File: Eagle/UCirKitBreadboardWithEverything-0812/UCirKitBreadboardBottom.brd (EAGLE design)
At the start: 64.8 x 99.4 mm, 900 parts

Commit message: 100% Bottom PCB
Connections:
- removed net 0_1439393321: JP661.P$2
- removed net 0_1439394245: JP601.P$2
- removed net N$1000: JP1000.P$2
- removed net N$1001: JP1001.P$2
- removed net N$1002: JP1002.P$2
- removed net N$1003: JP1003.P$2
- removed net N$1004: JP1004.P$2
- removed net N$1007: JP1007.P$2
- removed net N$1008: JP1008.P$2
- removed net N$1009: JP1009.P$2
- removed net N$1010: JP1010.P$2
- removed net N$1011: JP1011.P$2
- removed net N$1012: JP1012.P$2
- removed net N$1013: JP1013.P$2
- removed net N$1014: JP1014.P$2
- removed net N$1015: JP1015.P$2
- removed net N$1016: JP1016.P$2
- removed net N$1017: JP1017.P$2
- removed net N$1018: JP1018.P$2
- removed net N$1019: JP1019.P$2
- removed net N$1020: JP1020.P$2
- removed net N$1021: JP1021.P$2
- removed net N$1022: JP1022.P$2
- removed net N$1023: JP1023.P$2
- removed net N$1024: JP1024.P$2
- removed net N$1025: JP1025.P$2
- removed net N$1026: JP1026.P$2
- removed net N$1027: JP1027.P$2
- removed net N$1028: JP1028.P$2
- removed net N$1029: JP1029.P$2
- removed net N$1030: JP1030.P$2
- removed net N$1031: JP1031.P$2
- removed net N$1032: JP1032.P$2
- removed net N$1033: JP1033.P$2
- removed net N$1034: JP1034.P$2
- removed net N$1035: JP1035.P$2
- removed net N$1036: JP1036.P$2
- removed net N$1037: JP1037.P$2
- removed net N$1038: JP1038.P$2
- removed net N$1039: JP1039.P$2
- removed net N$1040: JP1040.P$2
- removed net N$1041: JP1041.P$2
- removed net N$1042: JP1042.P$2
- removed net N$1043: JP1043.P$2
- removed net N$1044: JP1044.P$2
- removed net N$1045: JP1045.P$2
- removed net N$1046: JP1046.P$2
- removed net N$1047: JP1047.P$2
- removed net N$1048: JP1048.P$2
- removed net N$1049: JP1049.P$2
- removed net N$1050: JP1050.P$2
- removed net N$1051: JP1051.P$2
- removed net N$1052: JP1052.P$2
- removed net N$1053: JP1053.P$2
- removed net N$1054: JP1054.P$2
- removed net N$1055: JP1055.P$2
- removed net N$1056: JP1056.P$2
- removed net N$1057: JP1057.P$2
- removed net N$1058: JP1058.P$2
- removed net N$1059: JP1059.P$2
- removed net N$1060: JP1060.P$2
- removed net N$1061: JP1061.P$2
- removed net N$1062: JP1062.P$2
- removed net N$1063: JP1063.P$2
- removed net N$1064: JP1064.P$2
- removed net N$1065: JP1065.P$2
- removed net N$1066: JP1066.P$2
- removed net N$1067: JP1067.P$2
- removed net N$1068: JP1068.P$2
- removed net N$1069: JP1069.P$2
- removed net N$1070: JP1070.P$2
- removed net N$1071: JP1071.P$2
- removed net N$1072: JP1072.P$2
- removed net N$1073: JP1073.P$2
- removed net N$1074: JP1074.P$2
- removed net N$1075: JP1075.P$2
- removed net N$1076: JP1076.P$2
- removed net N$1077: JP1077.P$2
- removed net N$1078: JP1078.P$2
- removed net N$1079: JP1079.P$2
- removed net N$1080: JP1080.P$2
- removed net N$1081: JP1081.P$2
- removed net N$1082: JP1082.P$2
- removed net N$1083: JP1083.P$2
- removed net N$1084: JP1084.P$2
- removed net N$1085: JP1085.P$2
- removed net N$1086: JP1086.P$2
- removed net N$1087: JP1087.P$2
- removed net N$1088: JP1088.P$2
- removed net N$1089: JP1089.P$2
- removed net N$1090: JP1090.P$2
- removed net N$1091: JP1091.P$2
- removed net N$1092: JP1092.P$2
- removed net N$1093: JP1093.P$2
- removed net N$1094: JP1094.P$2
- removed net N$1095: JP1095.P$2
- removed net N$1096: JP1096.P$2
- removed net N$1097: JP1097.P$2
- removed net N$1098: JP1098.P$2
- removed net N$1099: JP1099.P$2
- removed net N$1100: JP1100.P$2
- removed net N$1101: JP1101.P$2
- removed net N$1102: JP1102.P$2
- removed net N$1103: JP1103.P$2
- removed net N$1104: JP1104.P$2
- removed net N$1105: JP1105.P$2
- removed net N$1106: JP1106.P$2
- removed net N$1107: JP1107.P$2
- removed net N$1108: JP1108.P$2
- removed net N$1109: JP1109.P$2
- removed net N$1110: JP1110.P$2
- removed net N$1111: JP1111.P$2
- removed net N$1112: JP1112.P$2
- removed net N$1113: JP1113.P$2
- removed net N$1114: JP1114.P$2
- removed net N$1115: JP1115.P$2
- removed net N$1116: JP1116.P$2
- removed net N$1117: JP1117.P$2
- removed net N$1118: JP1118.P$2
- removed net N$1119: JP1119.P$2
- removed net N$1120: JP1120.P$2
- removed net N$1121: JP1121.P$2
- removed net N$1122: JP1122.P$2
- removed net N$1123: JP1123.P$2
- removed net N$1124: JP1124.P$2
- removed net N$1125: JP1125.P$2
- removed net N$1126: JP1126.P$2
- removed net N$1127: JP1127.P$2
- removed net N$1128: JP1128.P$2
- removed net N$1129: JP1129.P$2
- removed net N$1130: JP1130.P$2
- removed net N$1131: JP1131.P$2
- removed net N$1132: JP1132.P$2
- removed net N$1133: JP1133.P$2
- removed net N$1134: JP1134.P$2
- removed net N$1135: JP1135.P$2
- removed net N$1136: JP1136.P$2
- removed net N$1137: JP1137.P$2
- removed net N$1138: JP1138.P$2
- removed net N$1139: JP1139.P$2
- removed net N$1140: JP1140.P$2
- removed net N$1141: JP1141.P$2
- removed net N$1142: JP1142.P$2
- removed net N$1143: JP1143.P$2
- removed net N$1144: JP1144.P$2
- removed net N$1145: JP1145.P$2
- removed net N$1146: JP1146.P$2
- removed net N$1147: JP1147.P$2
- removed net N$1148: JP1148.P$2
- removed net N$1149: JP1149.P$2
- removed net N$1150: JP1150.P$2
- removed net N$1151: JP1151.P$2
- removed net N$1152: JP1152.P$2
- removed net N$1153: JP1153.P$2
- removed net N$1154: JP1154.P$2
- removed net N$1155: JP1155.P$2
- removed net N$1156: JP1156.P$2
- removed net N$1157: JP1157.P$2
- removed net N$1158: JP1158.P$2
- removed net N$1159: JP1159.P$2
- removed net N$1160: JP1160.P$2
- removed net N$1161: JP1161.P$2
- removed net N$1162: JP1162.P$2
- removed net N$1163: JP1163.P$2
- removed net N$1164: JP1164.P$2
- removed net N$1165: JP1165.P$2
- removed net N$1166: JP1166.P$2
- removed net N$1167: JP1167.P$2
- removed net N$1168: JP1168.P$2
- removed net N$1169: JP1169.P$2
- removed net N$1170: JP1170.P$2
- removed net N$1171: JP1171.P$2
- removed net N$1172: JP1172.P$2
- removed net N$1173: JP1173.P$2
- removed net N$1174: JP1174.P$2
- removed net N$1175: JP1175.P$2
- removed net N$1176: JP1176.P$2
- removed net N$1177: JP1177.P$2
- removed net N$1178: JP1178.P$2
- removed net N$1179: JP1179.P$2
- removed net N$1180: JP1180.P$2
- removed net N$1181: JP1181.P$2
- removed net N$1182: JP1182.P$2
- removed net N$1183: JP1183.P$2
- removed net N$1184: JP1184.P$2
- removed net N$1185: JP1185.P$2
- removed net N$1186: JP1186.P$2
- removed net N$1187: JP1187.P$2
- removed net N$1188: JP1188.P$2
- removed net N$1189: JP1189.P$2
- removed net N$1190: JP1190.P$2
- removed net N$1191: JP1191.P$2
- removed net N$1192: JP1192.P$2
- removed net N$1193: JP1193.P$2
- removed net N$1194: JP1194.P$2
- removed net N$1195: JP1195.P$2
- removed net N$1196: JP1196.P$2
- removed net N$1197: JP1197.P$2
- removed net N$1198: JP1198.P$2
- removed net N$1199: JP1199.P$2
- removed net N$1200: JP1200.P$2
- removed net N$902: JP902.P$2
- removed net N$903: JP903.P$2
- removed net N$904: JP904.P$2
- removed net N$905: JP905.P$2
- removed net N$906: JP906.P$2
- removed net N$907: JP907.P$2
- removed net N$908: JP908.P$2
- removed net N$909: JP909.P$2
- removed net N$910: JP910.P$2
- removed net N$911: JP911.P$2
- removed net N$912: JP912.P$2
- removed net N$913: JP913.P$2
- removed net N$914: JP914.P$2
- removed net N$915: JP915.P$2
- removed net N$916: JP916.P$2
- removed net N$917: JP917.P$2
- removed net N$918: JP918.P$2
- removed net N$919: JP919.P$2
- removed net N$920: JP920.P$2
- removed net N$921: JP921.P$2
- removed net N$922: JP922.P$2
- removed net N$923: JP923.P$2
- removed net N$924: JP924.P$2
- removed net N$925: JP925.P$2
- removed net N$926: JP926.P$2
- removed net N$927: JP927.P$2
- removed net N$928: JP928.P$2
- removed net N$929: JP929.P$2
- removed net N$930: JP930.P$2
- removed net N$931: JP931.P$2
- removed net N$932: JP932.P$2
- removed net N$933: JP933.P$2
- removed net N$934: JP934.P$2
- removed net N$935: JP935.P$2
- removed net N$936: JP936.P$2
- removed net N$937: JP937.P$2
- removed net N$938: JP938.P$2
- removed net N$939: JP939.P$2
- removed net N$940: JP940.P$2
- removed net N$941: JP941.P$2
- removed net N$942: JP942.P$2
- removed net N$943: JP943.P$2
- removed net N$944: JP944.P$2
- removed net N$945: JP945.P$2
- removed net N$946: JP946.P$2
- removed net N$947: JP947.P$2
- removed net N$948: JP948.P$2
- removed net N$949: JP949.P$2
- removed net N$950: JP950.P$2
- removed net N$951: JP951.P$2
- removed net N$952: JP952.P$2
- removed net N$953: JP953.P$2
- removed net N$954: JP954.P$2
- removed net N$955: JP955.P$2
- removed net N$956: JP956.P$2
- removed net N$957: JP957.P$2
- removed net N$958: JP958.P$2
- removed net N$959: JP959.P$2
- removed net N$960: JP960.P$2
- removed net N$962: JP962.P$2
- removed net N$963: JP963.P$2
- removed net N$964: JP964.P$2
- removed net N$965: JP965.P$2
- removed net N$966: JP966.P$2
- removed net N$967: JP967.P$2
- removed net N$968: JP968.P$2
- removed net N$969: JP969.P$2
- removed net N$970: JP970.P$2
- removed net N$971: JP971.P$2
- removed net N$972: JP972.P$2
- removed net N$973: JP973.P$2
- removed net N$974: JP974.P$2
- removed net N$975: JP975.P$2
- removed net N$976: JP976.P$2
- removed net N$977: JP977.P$2
- removed net N$978: JP978.P$2
- removed net N$979: JP979.P$2
- removed net N$980: JP980.P$2
- removed net N$981: JP981.P$2
- removed net N$982: JP982.P$2
- removed net N$983: JP983.P$2
- removed net N$984: JP984.P$2
- removed net N$985: JP985.P$2
- removed net N$986: JP986.P$2
- removed net N$987: JP987.P$2
- removed net N$988: JP988.P$2
- removed net N$989: JP989.P$2
- removed net N$990: JP990.P$2
- removed net N$991: JP991.P$2
- removed net N$992: JP992.P$2
- removed net N$993: JP993.P$2
- removed net N$994: JP994.P$2
- removed net N$995: JP995.P$2
- removed net N$996: JP996.P$2
- removed net N$997: JP997.P$2
- removed net N$998: JP998.P$2
- removed net N$999: JP999.P$2
- net 0_1439393083: now also JP1019.P$2
- net 0_1439393096: now also JP1017.P$2
- net 0_1439393111: now also JP1015.P$2
- net 0_1439393132: now also JP1005.P$2
- net 0_1439393222: now also JP1013.P$2
- net 0_1439393235: now also JP1011.P$2
- net 0_1439393247: now also JP1009.P$2
- net 0_1439393259: now also JP1007.P$2
- net 0_1439393301: now also JP1006.P$2
- net 0_1439393535: now also JP1003.P$2
- net 0_1439393546: now also JP1001.P$2
- net 0_1439393557: now also JP999.P$2
- net 0_1439393568: now also JP997.P$2
- net 0_1439393578: now also JP995.P$2
- net 0_1439393590: now also JP993.P$2
- net 0_1439393601: now also JP991.P$2
- net 0_1439393611: now also JP989.P$2
- net 0_1439393621: now also JP987.P$2
- net 0_1439393632: now also JP985.P$2
- net 0_1439393643: now also JP983.P$2
- net 0_1439393653: now also JP981.P$2
- net 0_1439393662: now also JP979.P$2
- net 0_1439393672: now also JP977.P$2
- net 0_1439393682: now also JP975.P$2
- net 0_1439393692: now also JP973.P$2
- net 0_1439393702: now also JP971.P$2
- net 0_1439393713: now also JP969.P$2
- net 0_1439393723: now also JP967.P$2
- net 0_1439393733: now also JP965.P$2
- net 0_1439393743: now also JP963.P$2
- net 0_1439393751: now also JP962.P$2
- net 0_1439394322: now also JP1141.P$2
- net 0_1439394368: now also JP1021.P$2
- net 0_1439394379: now also JP1023.P$2
- net 0_1439394391: now also JP1025.P$2
- net 0_1439394441: now also JP1027.P$2
- net 0_1439394451: now also JP1029.P$2
- net 0_1439394459: now also JP1031.P$2
- net 0_1439394467: now also JP1033.P$2
- net 0_1439394476: now also JP1035.P$2
- net 0_1439394485: now also JP1037.P$2
- net 0_1439394493: now also JP1039.P$2
- net 0_1439394502: now also JP1041.P$2
- net 0_1439394512: now also JP1043.P$2
- net 0_1439394521: now also JP1045.P$2
- net 0_1439394528: now also JP1047.P$2
- net 0_1439394536: now also JP1049.P$2
- net 0_1439394545: now also JP1051.P$2
- net 0_1439394554: now also JP1053.P$2
- net 0_1439394565: now also JP1055.P$2
- net 0_1439394575: now also JP1057.P$2
- net 0_1439394583: now also JP1059.P$2
- net 0_1439394592: now also JP1061.P$2
- net 0_1439394601: now also JP1063.P$2
- net 0_1439394609: now also JP1065.P$2
- net 0_1439394617: now also JP1067.P$2
- net 0_1439394705: now also JP1069.P$2
- net 0_1439394717: now also JP1071.P$2
- net 0_1439394727: now also JP1073.P$2
- net 0_1439394736: now also JP1075.P$2
- net 0_1439394745: now also JP1077.P$2
- net 0_1439394755: now also JP1079.P$2
- net 0_1439394769: now also JP1181.P$2
- net 0_1439394798: now also JP1161.P$2
- net 0_1439394824: now also JP1191.P$2
- net 0_1439394861: now also JP902.P$2
- net 0_1439394997: now also JP1081.P$2
- net 10_1439394322: now also JP1151.P$2
- net 10_1439394798: now also JP1171.P$2
- net 10_1439394861: now also JP912.P$2
- net 10_1439394997: now also JP1091.P$2
- net 11_1439394322: now also JP1152.P$2
- net 11_1439394798: now also JP1172.P$2
- net 11_1439394861: now also JP913.P$2
- net 11_1439394997: now also JP1092.P$2
- net 12_1439394322: now also JP1153.P$2
- net 12_1439394798: now also JP1173.P$2
- net 12_1439394861: now also JP914.P$2
- net 12_1439394997: now also JP1093.P$2
- net 13_1439394322: now also JP1154.P$2
- net 13_1439394798: now also JP1174.P$2
- net 13_1439394861: now also JP915.P$2
- net 13_1439394997: now also JP1094.P$2
- net 14_1439394322: now also JP1155.P$2
- net 14_1439394798: now also JP1175.P$2
- net 14_1439394861: now also JP916.P$2
- net 14_1439394997: now also JP1095.P$2
- net 15_1439394322: now also JP1156.P$2
- net 15_1439394798: now also JP1176.P$2
- net 15_1439394861: now also JP917.P$2
- net 15_1439394997: now also JP1096.P$2
- net 16_1439394322: now also JP1157.P$2
- net 16_1439394798: now also JP1177.P$2
- net 16_1439394861: now also JP918.P$2
- net 16_1439394997: now also JP1097.P$2
- net 17_1439394322: now also JP1158.P$2
- net 17_1439394798: now also JP1178.P$2
- net 17_1439394861: now also JP919.P$2
- net 17_1439394997: now also JP1098.P$2
- net 18_1439394322: now also JP1159.P$2
- net 18_1439394798: now also JP1179.P$2
- net 18_1439394861: now also JP920.P$2
- net 18_1439394997: now also JP1099.P$2
- net 19_1439394322: now also JP1160.P$2
- net 19_1439394798: now also JP1180.P$2
- net 19_1439394861: now also JP921.P$2
- net 19_1439394997: now also JP1100.P$2
- net 1_1439393083: now also JP1020.P$2
- net 1_1439393096: now also JP1018.P$2
- net 1_1439393111: now also JP1016.P$2
- net 1_1439393222: now also JP1014.P$2
- net 1_1439393235: now also JP1012.P$2
- net 1_1439393247: now also JP1010.P$2
- net 1_1439393259: now also JP1008.P$2
- net 1_1439393535: now also JP1004.P$2
- net 1_1439393546: now also JP1002.P$2
- net 1_1439393557: now also JP1000.P$2
- net 1_1439393568: now also JP998.P$2
- net 1_1439393578: now also JP996.P$2
- net 1_1439393590: now also JP994.P$2
- net 1_1439393601: now also JP992.P$2
- net 1_1439393611: now also JP990.P$2
- net 1_1439393621: now also JP988.P$2
- net 1_1439393632: now also JP986.P$2
- net 1_1439393643: now also JP984.P$2
- net 1_1439393653: now also JP982.P$2
- net 1_1439393662: now also JP980.P$2
- net 1_1439393672: now also JP978.P$2
- net 1_1439393682: now also JP976.P$2
- net 1_1439393692: now also JP974.P$2
- net 1_1439393702: now also JP972.P$2
- net 1_1439393713: now also JP970.P$2
- net 1_1439393723: now also JP968.P$2
- net 1_1439393733: now also JP966.P$2
- net 1_1439393743: now also JP964.P$2
- net 1_1439394322: now also JP1142.P$2
- net 1_1439394368: now also JP1022.P$2
- net 1_1439394379: now also JP1024.P$2
- net 1_1439394391: now also JP1026.P$2
- net 1_1439394441: now also JP1028.P$2
- net 1_1439394451: now also JP1030.P$2
- net 1_1439394459: now also JP1032.P$2
- net 1_1439394467: now also JP1034.P$2
- net 1_1439394476: now also JP1036.P$2
- net 1_1439394485: now also JP1038.P$2
- net 1_1439394493: now also JP1040.P$2
- net 1_1439394502: now also JP1042.P$2
- net 1_1439394512: now also JP1044.P$2
- net 1_1439394521: now also JP1046.P$2
- net 1_1439394528: now also JP1048.P$2
- net 1_1439394536: now also JP1050.P$2
- net 1_1439394545: now also JP1052.P$2
- net 1_1439394554: now also JP1054.P$2
- net 1_1439394565: now also JP1056.P$2
- net 1_1439394575: now also JP1058.P$2
- net 1_1439394583: now also JP1060.P$2
- net 1_1439394592: now also JP1062.P$2
- net 1_1439394601: now also JP1064.P$2
- net 1_1439394609: now also JP1066.P$2
- net 1_1439394617: now also JP1068.P$2
- net 1_1439394705: now also JP1070.P$2
- net 1_1439394717: now also JP1072.P$2
- net 1_1439394727: now also JP1074.P$2
- net 1_1439394736: now also JP1076.P$2
- net 1_1439394745: now also JP1078.P$2
- net 1_1439394755: now also JP1080.P$2
- net 1_1439394769: now also JP1182.P$2
- net 1_1439394798: now also JP1162.P$2
- net 1_1439394824: now also JP1192.P$2
- net 1_1439394861: now also JP903.P$2
- net 1_1439394997: now also JP1082.P$2
- net 20_1439394861: now also JP922.P$2
- net 20_1439394997: now also JP1101.P$2
- net 21_1439394861: now also JP923.P$2
- net 21_1439394997: now also JP1102.P$2
- net 22_1439394861: now also JP924.P$2
- net 22_1439394997: now also JP1103.P$2
- net 23_1439394861: now also JP925.P$2
- net 23_1439394997: now also JP1104.P$2
- net 24_1439394861: now also JP926.P$2
- net 24_1439394997: now also JP1105.P$2
- net 25_1439394861: now also JP927.P$2
- net 25_1439394997: now also JP1106.P$2
- net 26_1439394861: now also JP928.P$2
- net 26_1439394997: now also JP1107.P$2
- net 27_1439394861: now also JP929.P$2
- net 27_1439394997: now also JP1108.P$2
- net 28_1439394861: now also JP930.P$2
- net 28_1439394997: now also JP1109.P$2
- net 29_1439394861: now also JP931.P$2
- net 29_1439394997: now also JP1110.P$2
- net 2_1439394322: now also JP1143.P$2
- net 2_1439394769: now also JP1183.P$2
- net 2_1439394798: now also JP1163.P$2
- net 2_1439394824: now also JP1193.P$2
- net 2_1439394861: now also JP904.P$2
- net 2_1439394997: now also JP1083.P$2
- net 30_1439394861: now also JP932.P$2
- net 30_1439394997: now also JP1111.P$2
- net 31_1439394861: now also JP933.P$2
- net 31_1439394997: now also JP1112.P$2
- net 32_1439394861: now also JP934.P$2
- net 32_1439394997: now also JP1113.P$2
- net 33_1439394861: now also JP935.P$2
- net 33_1439394997: now also JP1114.P$2
- net 34_1439394861: now also JP936.P$2
- net 34_1439394997: now also JP1115.P$2
- net 35_1439394861: now also JP937.P$2
- net 35_1439394997: now also JP1116.P$2
- net 36_1439394861: now also JP938.P$2
- net 36_1439394997: now also JP1117.P$2
- net 37_1439394861: now also JP939.P$2
- net 37_1439394997: now also JP1118.P$2
- net 38_1439394861: now also JP940.P$2
- net 38_1439394997: now also JP1119.P$2
- net 39_1439394861: now also JP941.P$2
- net 39_1439394997: now also JP1120.P$2
- net 3_1439394322: now also JP1144.P$2
- net 3_1439394769: now also JP1184.P$2
- net 3_1439394798: now also JP1164.P$2
- net 3_1439394824: now also JP1194.P$2
- net 3_1439394861: now also JP905.P$2
- net 3_1439394997: now also JP1084.P$2
- net 40_1439394861: now also JP942.P$2
- net 40_1439394997: now also JP1121.P$2
- net 41_1439394861: now also JP943.P$2
- net 41_1439394997: now also JP1122.P$2
- net 42_1439394861: now also JP944.P$2
- net 42_1439394997: now also JP1123.P$2
- net 43_1439394861: now also JP945.P$2
- net 43_1439394997: now also JP1124.P$2
- net 44_1439394861: now also JP946.P$2
- net 44_1439394997: now also JP1125.P$2
- net 45_1439394861: now also JP947.P$2
- net 45_1439394997: now also JP1126.P$2
- net 46_1439394861: now also JP948.P$2
- net 46_1439394997: now also JP1127.P$2
- net 47_1439394861: now also JP949.P$2
- net 47_1439394997: now also JP1128.P$2
- net 48_1439394861: now also JP950.P$2
- net 48_1439394997: now also JP1129.P$2
- net 49_1439394861: now also JP951.P$2
- net 49_1439394997: now also JP1130.P$2
- net 4_1439394322: now also JP1145.P$2
- net 4_1439394769: now also JP1185.P$2
- net 4_1439394798: now also JP1165.P$2
- net 4_1439394824: now also JP1195.P$2
- net 4_1439394861: now also JP906.P$2
- net 4_1439394997: now also JP1085.P$2
- net 50_1439394861: now also JP952.P$2
- net 50_1439394997: now also JP1131.P$2
- net 51_1439394861: now also JP953.P$2
- net 51_1439394997: now also JP1132.P$2
- net 52_1439394861: now also JP954.P$2
- net 52_1439394997: now also JP1133.P$2
- net 53_1439394861: now also JP955.P$2
- net 53_1439394997: now also JP1134.P$2
- net 54_1439394861: now also JP956.P$2
- net 54_1439394997: now also JP1135.P$2
- net 55_1439394861: now also JP957.P$2
- net 55_1439394997: now also JP1136.P$2
- net 56_1439394861: now also JP958.P$2
- net 56_1439394997: now also JP1137.P$2
- net 57_1439394861: now also JP959.P$2
- net 57_1439394997: now also JP1138.P$2
- net 58_1439394861: now also JP960.P$2
- net 58_1439394997: now also JP1139.P$2
- net 59_1439394997: now also JP1140.P$2
- net 5_1439394322: now also JP1146.P$2
- net 5_1439394769: now also JP1186.P$2
- net 5_1439394798: now also JP1166.P$2
- net 5_1439394824: now also JP1196.P$2
- net 5_1439394861: now also JP907.P$2
- net 5_1439394997: now also JP1086.P$2
- net 60_029414: now also JP601.P$2
- net 60_172194: no longer JP1006.P$2
- net 60_189984: no longer JP1005.P$2
- net 60_19999: now also JP661.P$2
- net 6_1439394322: now also JP1147.P$2
- net 6_1439394769: now also JP1187.P$2
- net 6_1439394798: now also JP1167.P$2
- net 6_1439394824: now also JP1197.P$2
- net 6_1439394861: now also JP908.P$2
- net 6_1439394997: now also JP1087.P$2
- net 7_1439394322: now also JP1148.P$2
- net 7_1439394769: now also JP1188.P$2
- net 7_1439394798: now also JP1168.P$2
- net 7_1439394824: now also JP1198.P$2
- net 7_1439394861: now also JP909.P$2
- net 7_1439394997: now also JP1088.P$2
- net 8_1439394322: now also JP1149.P$2
- net 8_1439394769: now also JP1189.P$2
- net 8_1439394798: now also JP1169.P$2
- net 8_1439394824: now also JP1199.P$2
- net 8_1439394861: now also JP910.P$2
- net 8_1439394997: now also JP1089.P$2
- net 9_1439394322: now also JP1150.P$2
- net 9_1439394769: now also JP1190.P$2
- net 9_1439394798: now also JP1170.P$2
- net 9_1439394824: now also JP1200.P$2
- net 9_1439394861: now also JP911.P$2
- net 9_1439394997: now also JP1090.P$2
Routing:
- net 16_1439394861: track 22.0 -> 73.4 mm
- net 35_1439394861: track 66.1 -> 28.9 mm, vias 0 -> 2
- net 57_1439394997: track 47.8 -> 83.7 mm, vias 0 -> 2
- net 3_1439394997: track 60.8 -> 27.9 mm, vias 0 -> 3
- net 23_1439394861: track 59.7 -> 27.1 mm, vias 2 -> 3
- net 45_1439394861: track 28.0 -> 58.1 mm, vias 2 -> 1
- net 43_1439394861: track 61.5 -> 31.7 mm, vias 0 -> 2
- net 57_1439394861: track 32.7 -> 62.2 mm, vias 4 -> 2
- net 6_1439394824: track 43.3 -> 14.1 mm, vias 0 -> 2
- net 56_1439394997: track 41.1 -> 70.0 mm
- net 31_1439394861: track 54.9 -> 26.3 mm
- net 48_1439394997: track 24.5 -> 53.0 mm, vias 2 -> 1
- net 54_1439394997: track 33.2 -> 59.7 mm
- net 21_1439394861: track 22.7 -> 48.4 mm, vias 2 -> 1
- net 54_1439394861: track 84.5 -> 60.4 mm
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
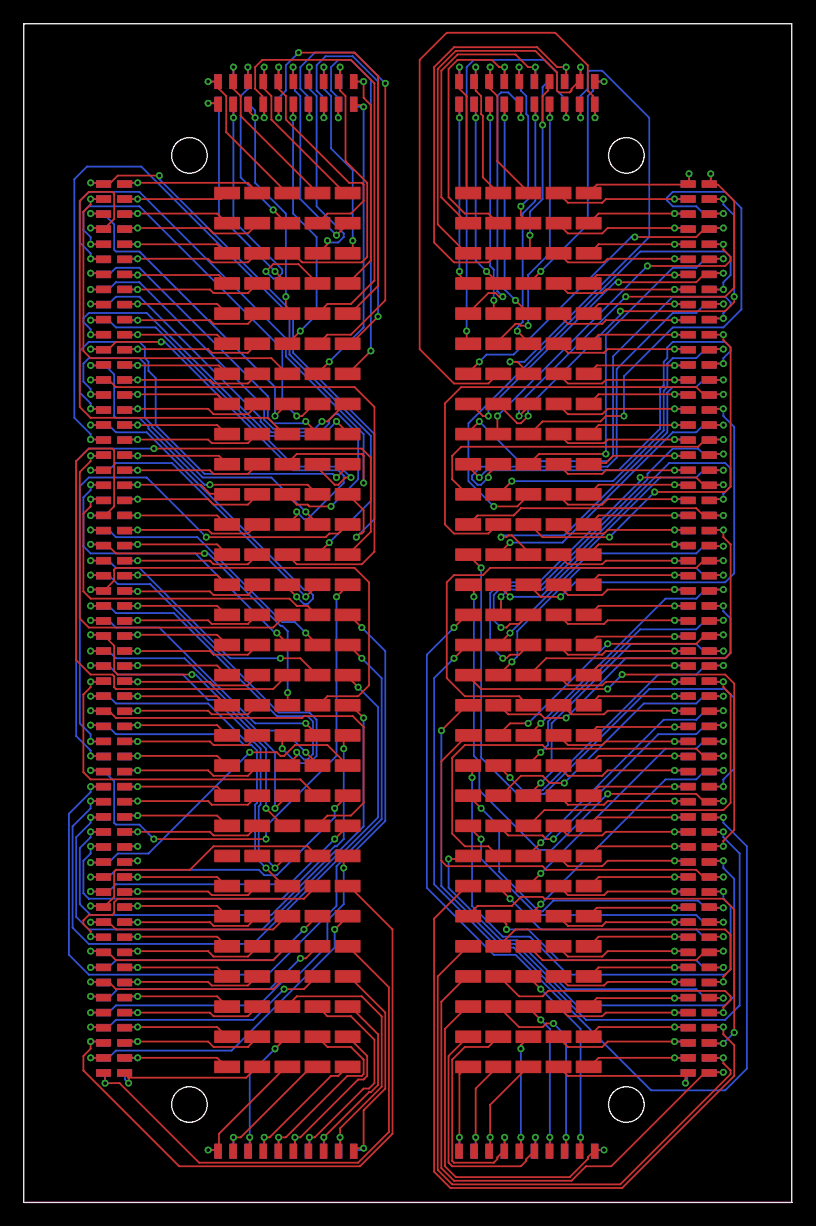
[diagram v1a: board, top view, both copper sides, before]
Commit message: UCirKitBreadboardBottom updated with wider width of central contact points
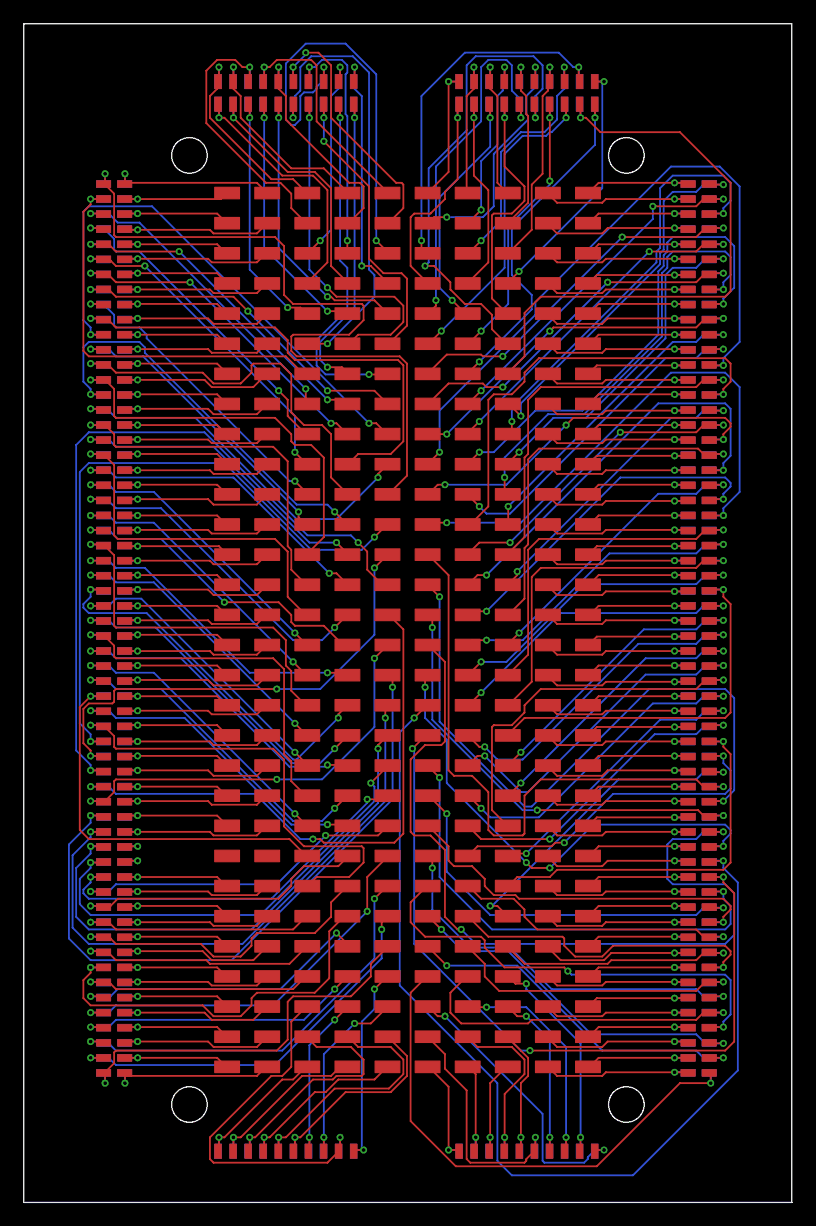
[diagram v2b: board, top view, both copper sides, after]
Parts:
- moved JP306 3.42 mm to (34.0, 85.1)
- moved JP316 3.42 mm to (34.0, 82.5)
- moved JP326 3.42 mm to (34.0, 80.0)
- moved JP336 3.42 mm to (34.0, 77.5)
- moved JP346 3.42 mm to (34.0, 74.9)
- moved JP356 3.42 mm to (34.0, 72.4)
- moved JP366 3.42 mm to (34.0, 69.8)
- moved JP376 3.42 mm to (34.0, 67.3)
- moved JP386 3.42 mm to (34.0, 64.8)
- moved JP396 3.42 mm to (34.0, 62.2)
- moved JP406 3.42 mm to (34.0, 59.7)
- moved JP416 3.42 mm to (34.0, 57.1)
- moved JP426 3.42 mm to (34.0, 54.6)
- moved JP436 3.42 mm to (34.0, 52.1)
- moved JP446 3.42 mm to (34.0, 49.5)
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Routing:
- net 16_1439394861: track 73.4 -> 26.8 mm
- net 57_1439394997: track 83.7 -> 38.3 mm, vias 2 -> 3
- net 53_1439394997: track 37.1 -> 66.0 mm, vias 1 -> 3
- net 54_1439394997: track 59.7 -> 87.9 mm
- net 4_1439394861: track 54.4 -> 28.3 mm, vias 2 -> 3
- net 19_1439394798: track 54.6 -> 29.7 mm, vias 1 -> 2
- net 54_1439394861: track 60.4 -> 35.6 mm, vias 2 -> 3
- net 21_1439394861: track 48.4 -> 24.9 mm, vias 1 -> 2
- net 48_1439394997: track 53.0 -> 30.0 mm, vias 1 -> 2
- net 45_1439394861: track 58.1 -> 35.2 mm, vias 1 -> 2
- net 12_1439394997: track 35.5 -> 58.1 mm
- net 46_1439394997: track 62.0 -> 39.6 mm, vias 1 -> 2
- net 22_1439394997: track 23.5 -> 45.9 mm, vias 1 -> 2
- net 55_1439394861: track 70.6 -> 48.8 mm
- net 57_1439394861: track 62.2 -> 41.3 mm, vias 2 -> 3
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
